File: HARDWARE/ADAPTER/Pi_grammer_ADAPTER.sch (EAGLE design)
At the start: 3 parts, among them J3 TESTBED, J4 CABLE

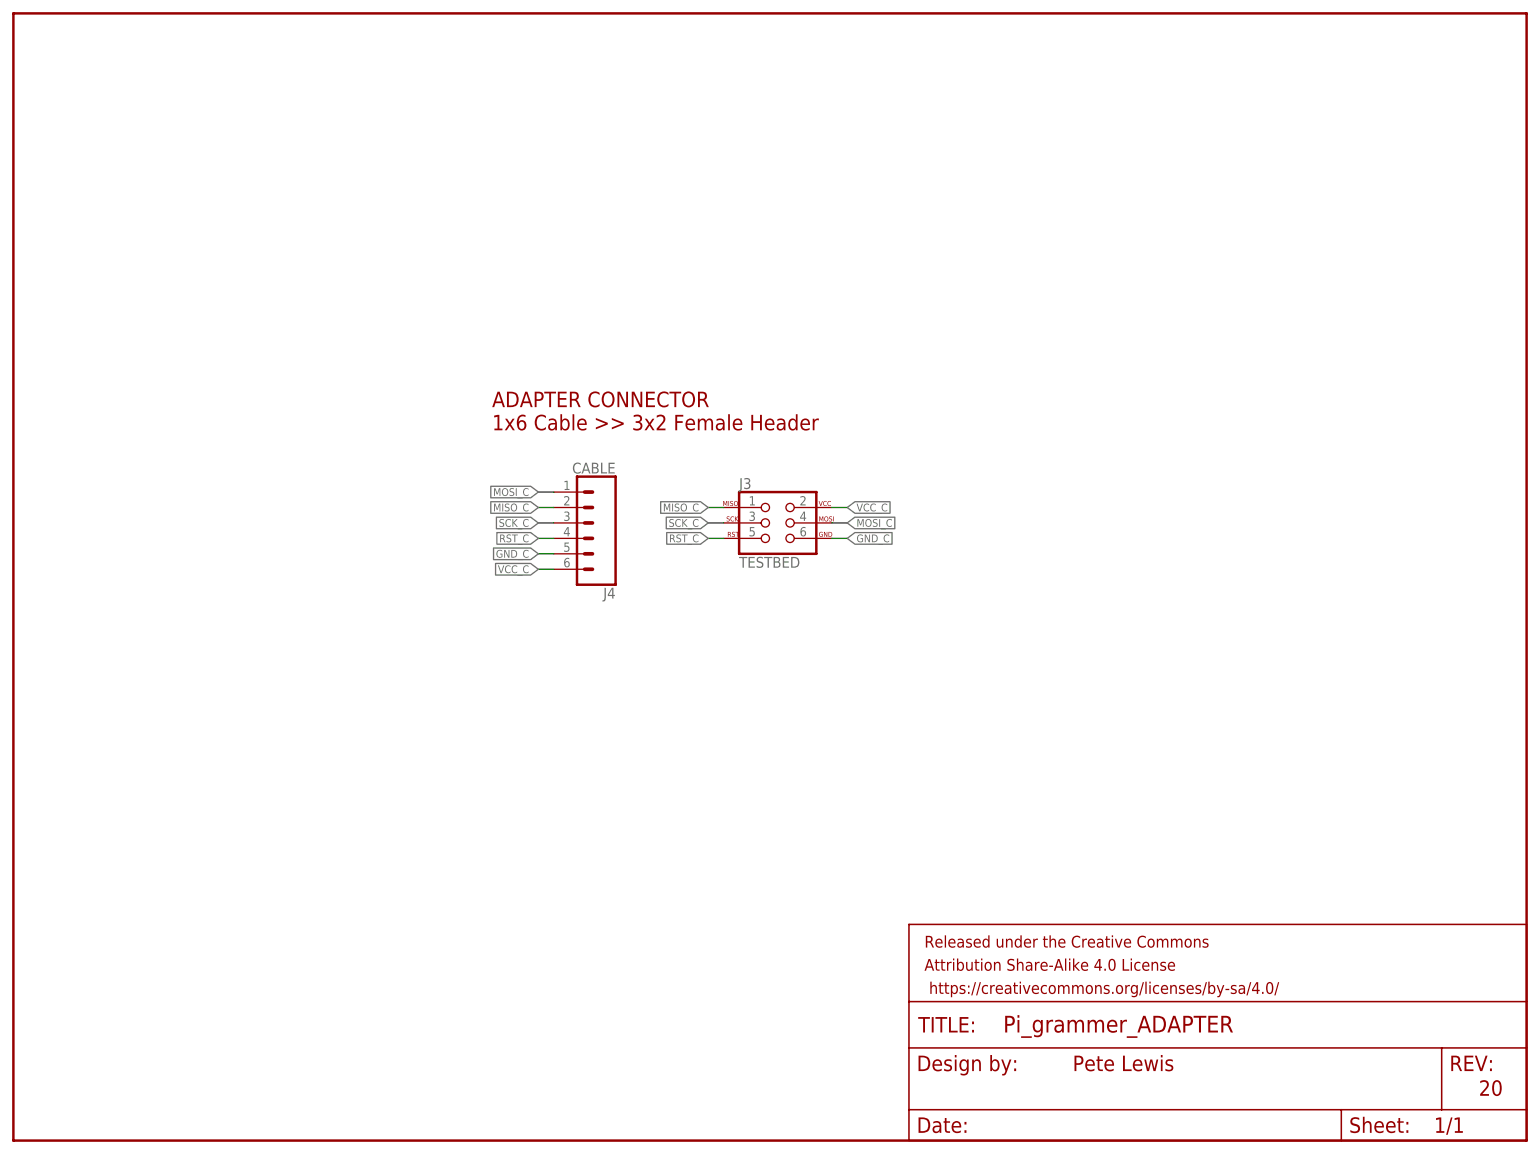
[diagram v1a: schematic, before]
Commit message: Adapter updates for storefront product
-Added open source hardware logo
-sparkfun flame
-"product" board name
-schematic cleanup
-removed rounded cornders for easier board de-panelization
-lengthened board to eliiminate overhaning parts
-moved to SMT parts for easier assembly
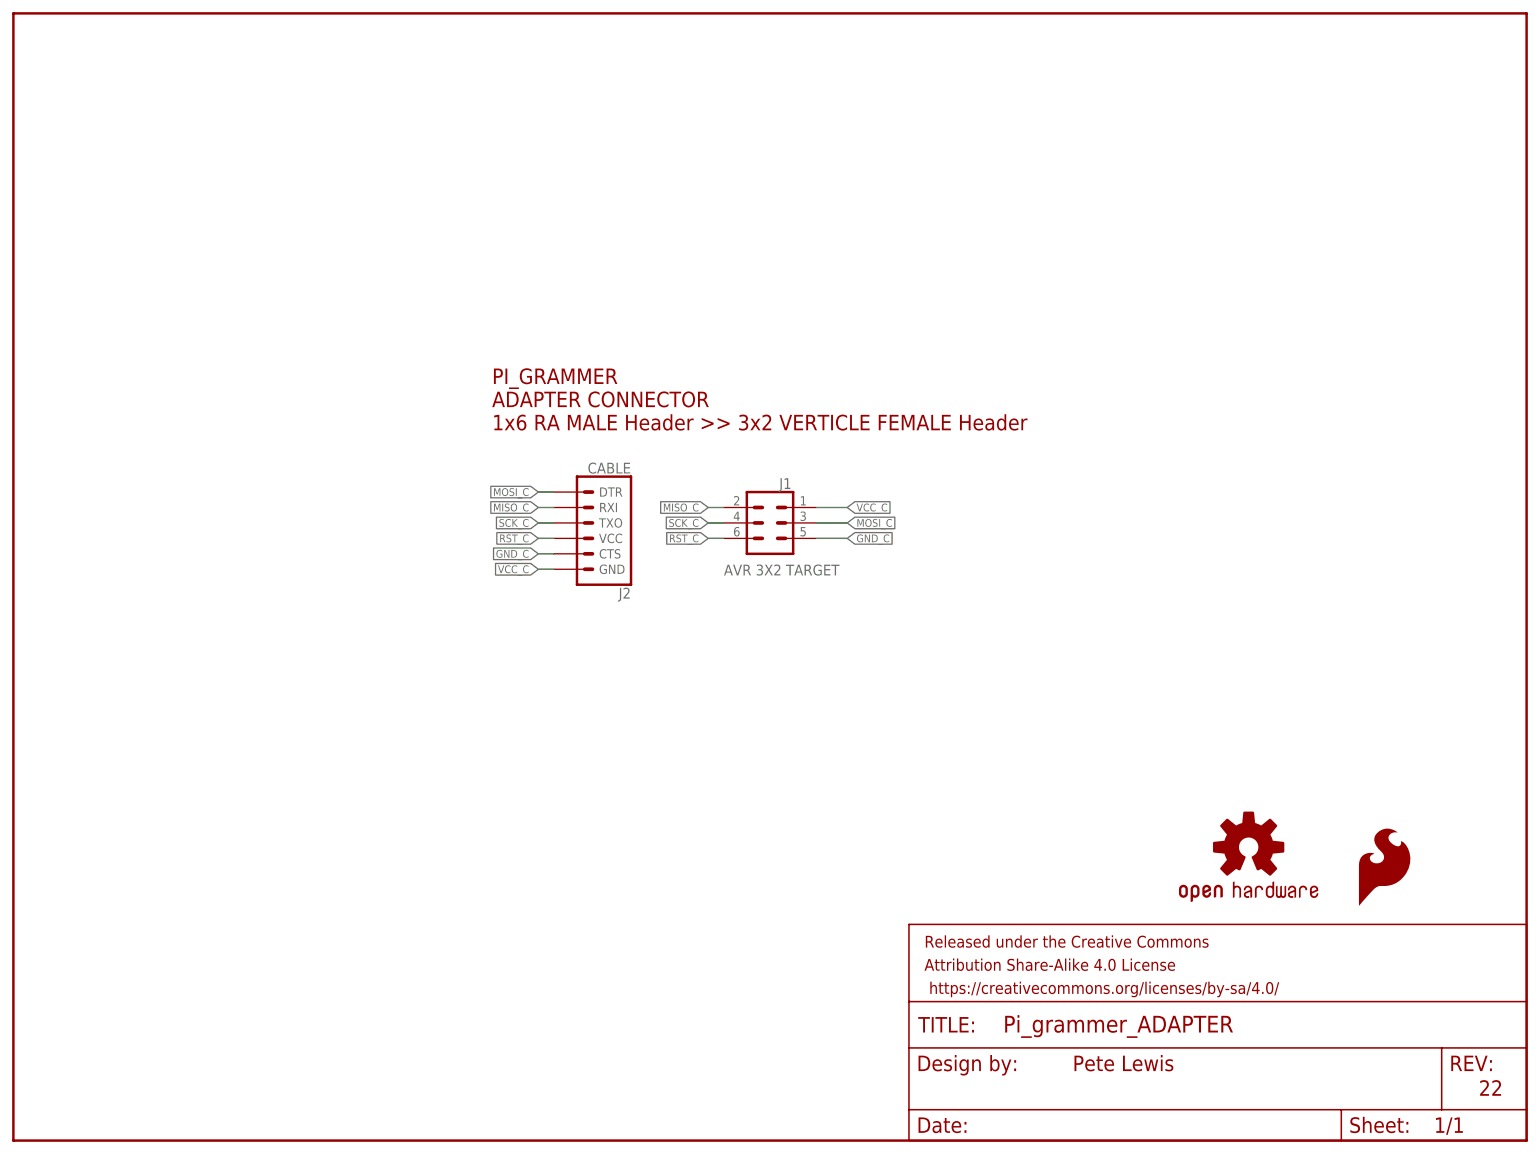
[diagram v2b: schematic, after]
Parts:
- removed J3: TESTBED, SparkFun-Connectors:AVR_SPI_PROG_3X22X3_LOCK
- removed J4: CABLE, SparkFun-Connectors:CONN_06RA_LOCK
- added J1: AVR 3X2 TARGET, SparkFun-Connectors:CONN_03X2SMT
- added J2: CABLE, SparkFun-Connectors:6_PIN_SERIAL_TARGETSMD
- added LOGO1: SFE_LOGO_FLAME.1_INCH, SparkFun-Aesthetics:SFE_LOGO_FLAME.1_INCH
- added LOGO2: OSHW-LOGOMINI, SparkFun-Aesthetics:OSHW-LOGOMINI
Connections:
- net GND_C: now also J1.5, J2.CTS; no longer J3.6, J4.5
- net MISO_C: now also J1.2, J2.RXI; no longer J3.1, J4.2
- net MOSI_C: now also J1.3, J2.DTR; no longer J3.4, J4.1
- net RST_C: now also J1.6, J2.VCC; no longer J3.5, J4.4
- net SCK_C: now also J1.4, J2.TXO; no longer J3.3, J4.3
- net VCC_C: now also J1.1, J2.GND; no longer J3.2, J4.6
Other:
- note added: "22"
- note added: "PI_GRAMMER ADAPTER CONNECTOR 1x6 RA MALE Header >> 3x2 VERTICLE FEMALE Header"
- note removed: "20"
- note removed: "ADAPTER CONNECTOR 1x6 Cable >> 3x2 Female Header"
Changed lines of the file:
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@@
 <layer number="230" name="230bmp" color="7" fill="1" visible="yes" active="yes"/>
 <layer number="231" name="231bmp" color="7" fill="1" visible="yes" active="yes"/>
+<layer number="232" name="Eagle3D_PG2" color="7" fill="1" visible="yes" active="yes"/>
+<layer number="233" name="Eagle3D_PG3" color="7" fill="1" visible="yes" active="yes"/>
 <layer number="248" name="Housing" color="7" fill="1" visible="yes" active="yes"/>
 <layer number="249" name="Edge" color="7" fill="1" visible="yes" active="yes"/>
@@
 </classes>
 <parts>
-<part name="J3" library="SparkFun-Connectors" deviceset="AVR_SPI_PROG_3X2" device="2X3_LOCK" value="TESTBED">
-<attribute name="PROD_ID" value="CONN-11566"/>
-</part>
-<part name="J4" library="SparkFun-Connectors" deviceset="CONN_06" device="RA_LOCK" value="CABLE">
+<part name="J2" library="SparkFun-Connectors" deviceset="6_PIN_SERIAL_TARGET" device="SMD" value="CABLE">
 <attribute name="PROD_ID" value="CONN-10140"/>
 </part>
 <part name="FRAME1" library="SparkFun-Aesthetics" deviceset="FRAME-LETTER" device=""/>
+<part name="J1" library="SparkFun-Connectors" deviceset="CONN_03X2" device="SMT" value="AVR 3X2 TARGET"/>
+<part name="LOGO1" library="SparkFun-Aesthetics" deviceset="SFE_LOGO_FLAME" device=".1_INCH"/>
+<part name="LOGO2" library="SparkFun-Aesthetics" deviceset="OSHW-LOGO" device="MINI"/>
 </parts>
 <sheets>
 <sheet>
 <plain>
-<text x="86.36" y="299.72" size="2.54" layer="94" font="vector">ADAPTER CONNECTOR
-1x6 Cable &gt;&gt; 3x2 Female Header</text>
+<text x="86.36" y="299.72" size="2.54" layer="94" font="vector">PI_GRAMMER
+ADAPTER CONNECTOR
+1x6 RA MALE Header &gt;&gt; 3x2 VERTICLE FEMALE Header</text>
 <text x="181.864" y="194.31" size="2.54" layer="94" font="vector">Pete Lewis</text>
-<text x="248.666" y="190.246" size="2.54" layer="94" font="vector">20</text>
+<text x="248.666" y="190.246" size="2.54" layer="94" font="vector">22</text>
 </plain>
 <instances>
-<instance part="J3" gate="G$1" x="132.08" y="284.48">
-<attribute name="PROD_ID" x="132.08" y="284.48" size="1.27" layer="96" display="off"/>
-</instance>
-<instance part="J4" gate="G$1" x="101.6" y="284.48" rot="R180">
+<instance part="J2" gate="G$1" x="101.6" y="284.48" rot="R180">
 <attribute name="PROD_ID" x="101.6" y="284.48" size="1.27" layer="96" rot="R180" display="off"/>
 </instance>
 <instance part="FRAME1" gate="G$1" x="7.62" y="182.88"/>
 <instance part="FRAME1" gate="V" x="154.94" y="182.88"/>
+<instance part="J1" gate="G$1" x="132.08" y="284.48" smashed="yes" rot="MR0">
+<attribute name="PROD_ID" x="132.08" y="284.48" size="1.27" layer="96" rot="MR0" display="off"/>
+<attribute name="NAME" x="135.636" y="290.068" size="1.778" layer="95" font="vector" rot="MR0"/>
+<attribute name="VALUE" x="143.51" y="277.622" size="1.778" layer="96" font="vector" rot="MR0" align="top-left"/>
+</instance>
+<instance part="LOGO1" gate="G$1" x="228.6" y="220.98"/>
+<instance part="LOGO2" gate="G$1" x="210.82" y="231.14"/>
 </instances>
 <busses>
@@
 <net name="MOSI_C" class="0">
 <segment>
-<pinref part="J4" gate="G$1" pin="1"/>
+<pinref part="J2" gate="G$1" pin="DTR"/>
 <wire x1="96.52" y1="289.56" x2="93.98" y2="289.56" width="0.1524" layer="91"/>
 <label x="93.98" y="289.56" size="1.27" layer="95" rot="R180" xref="yes"/>
 </segment>
 <segment>
-<pinref part="J3" gate="G$1" pin="4"/>
-<wire x1="142.24" y1="284.48" x2="144.78" y2="284.48" width="0.1524" layer="91"/>
+<wire x1="139.7" y1="284.48" x2="144.78" y2="284.48" width="0.1524" layer="91"/>
 <label x="144.78" y="284.48" size="1.27" layer="95" xref="yes"/>
+<pinref part="J1" gate="G$1" pin="3"/>
 </segment>
 </net>
 <net name="MISO_C" class="0">
 <segment>
-<pinref part="J4" gate="G$1" pin="2"/>
+<pinref part="J2" gate="G$1" pin="RXI"/>
 <wire x1="96.52" y1="287.02" x2="93.98" y2="287.02" width="0.1524" layer="91"/>
 <label x="93.98" y="287.02" size="1.27" layer="95" rot="R180" xref="yes"/>
 </segment>
 <segment>
-<pinref part="J3" gate="G$1" pin="1"/>
 <wire x1="124.46" y1="287.02" x2="121.92" y2="287.02" width="0.1524" layer="91"/>
 <label x="121.92" y="287.02" size="1.27" layer="95" rot="R180" xref="yes"/>
+<pinref part="J1" gate="G$1" pin="2"/>
 </segment>
 </net>
 <net name="SCK_C" class="0">
 <segment>
-<pinref part="J3" gate="G$1" pin="3"/>
 <wire x1="124.46" y1="284.48" x2="121.92" y2="284.48" width="0.1524" layer="91"/>
 <label x="121.92" y="284.48" size="1.27" layer="95" rot="R180" xref="yes"/>
+<pinref part="J1" gate="G$1" pin="4"/>
 </segment>
 <segment>
-<pinref part="J4" gate="G$1" pin="3"/>
+<pinref part="J2" gate="G$1" pin="TXO"/>
 <wire x1="96.52" y1="284.48" x2="93.98" y2="284.48" width="0.1524" layer="91"/>
 <label x="93.98" y="284.48" size="1.27" layer="95" rot="R180" xref="yes"/>
@@
 <net name="RST_C" class="0">
 <segment>
-<pinref part="J4" gate="G$1" pin="4"/>
+<pinref part="J2" gate="G$1" pin="VCC"/>
 <wire x1="96.52" y1="281.94" x2="93.98" y2="281.94" width="0.1524" layer="91"/>
 <label x="93.98" y="281.94" size="1.27" layer="95" rot="R180" xref="yes"/>
 </segment>
 <segment>
-<pinref part="J3" gate="G$1" pin="5"/>
 <wire x1="124.46" y1="281.94" x2="121.92" y2="281.94" width="0.1524" layer="91"/>
 <label x="121.92" y="281.94" size="1.27" layer="95" rot="R180" xref="yes"/>
+<pinref part="J1" gate="G$1" pin="6"/>
 </segment>
 </net>
 <net name="GND_C" class="0">
 <segment>
-<pinref part="J4" gate="G$1" pin="5"/>
+<pinref part="J2" gate="G$1" pin="CTS"/>
 <wire x1="96.52" y1="279.4" x2="93.98" y2="279.4" width="0.1524" layer="91"/>
 <label x="93.98" y="279.4" size="1.27" layer="95" rot="R180" xref="yes"/>
 </segment>
 <segment>
-<pinref part="J3" gate="G$1" pin="6"/>
-<wire x1="142.24" y1="281.94" x2="144.78" y2="281.94" width="0.1524" layer="91"/>
+<wire x1="139.7" y1="281.94" x2="144.78" y2="281.94" width="0.1524" layer="91"/>
 <label x="144.78" y="281.94" size="1.27" layer="95" xref="yes"/>
+<pinref part="J1" gate="G$1" pin="5"/>
 </segment>
 </net>
 <net name="VCC_C" class="0">
 <segment>
-<pinref part="J3" gate="G$1" pin="2"/>
-<wire x1="142.24" y1="287.02" x2="144.78" y2="287.02" width="0.1524" layer="91"/>
+<wire x1="139.7" y1="287.02" x2="144.78" y2="287.02" width="0.1524" layer="91"/>
 <label x="144.78" y="287.02" size="1.27" layer="95" xref="yes"/>
+<pinref part="J1" gate="G$1" pin="1"/>
 </segment>
 <segment>
-<pinref part="J4" gate="G$1" pin="6"/>
+<pinref part="J2" gate="G$1" pin="GND"/>
 <wire x1="96.52" y1="276.86" x2="93.98" y2="276.86" width="0.1524" layer="91"/>
 <label x="93.98" y="276.86" size="1.27" layer="95" rot="R180" xref="yes"/>
